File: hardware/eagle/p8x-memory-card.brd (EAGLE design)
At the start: 160 x 100 mm, 10 parts, among them J1 DIN41612-96M, U1 28C256-15, U2 62256-70, U3 74HCT245, U4 74HCT30, U5 74HCT138-DOE, U6 74HCT138-DLD, U7 74HCT00, U8 74HCT32, U9 74HCT08

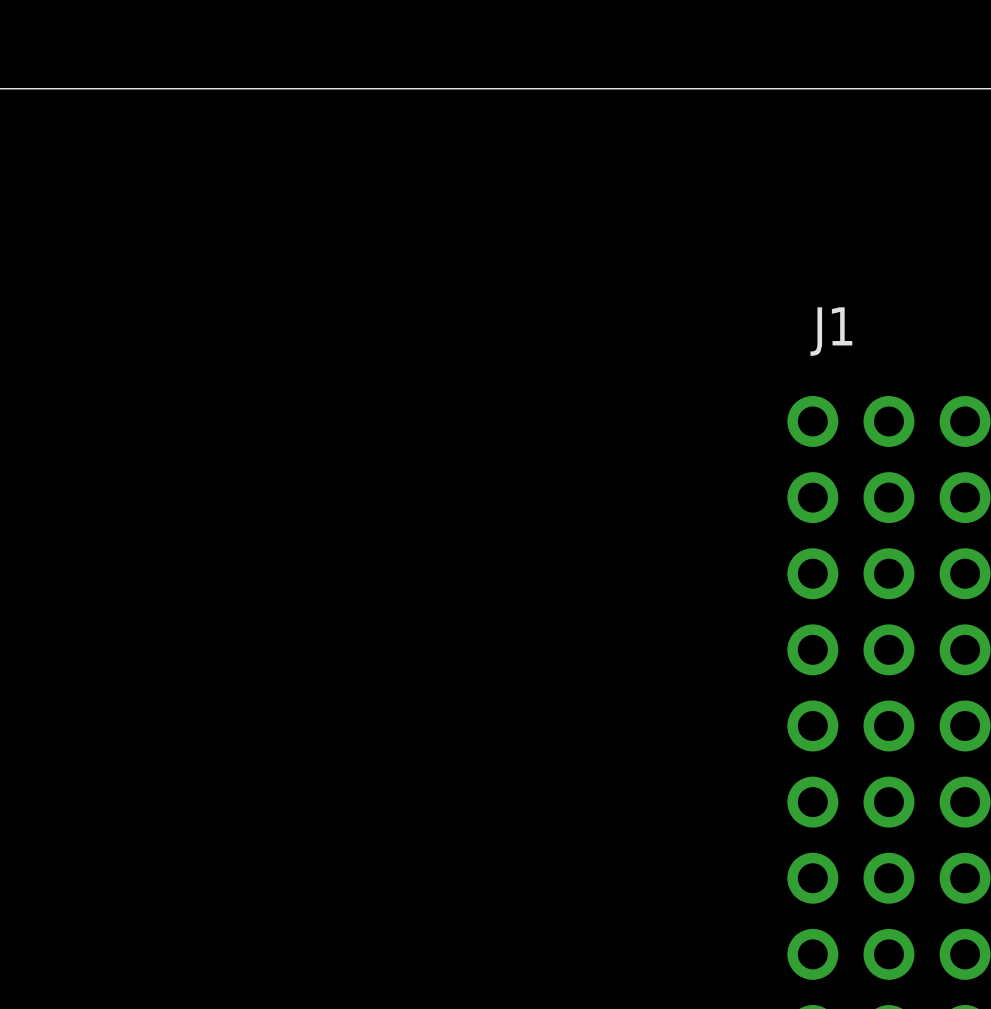
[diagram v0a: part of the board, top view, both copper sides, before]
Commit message: Memory card: ROM/RAM/RD/WR access LEDs replace SEL; traditional schematic PDFs; backlog + standards updates
- Select LEDs gated with -BOE (real accesses, not idle decode); spare U8/U9 gates as drivers
- Standards sec.9 allows finer-grained LED sets; fab checklist updated
- New traditional-style schematic PDFs + their render scripts (generators/)
- Backlog: DIN flange holes, board mounting holes, backplane PWR LED placement review
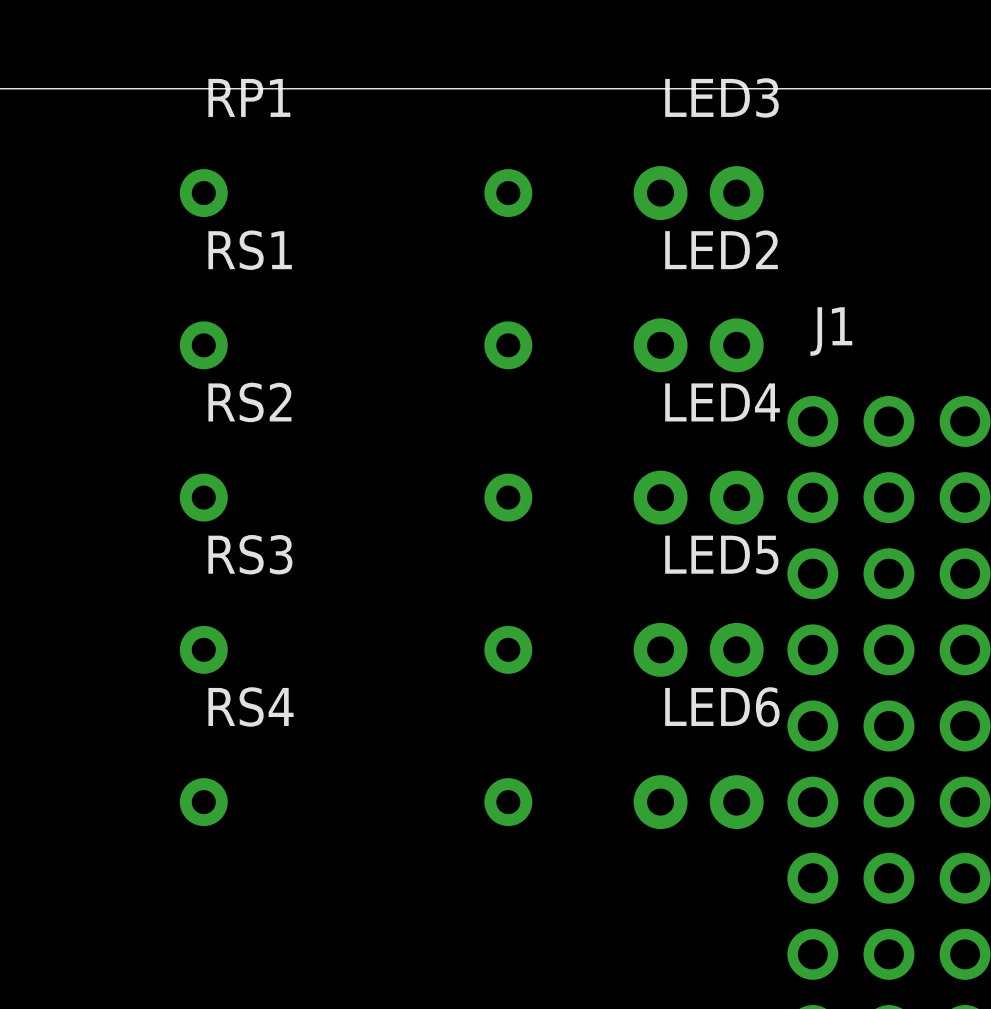
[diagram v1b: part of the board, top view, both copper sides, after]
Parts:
- added LED2: ROM-YEL, p8x:LED5
- added LED3: PWR-GRN, p8x:LED5
- added LED4: RAM-YEL, p8x:LED5
- added LED5: RD-GRN, p8x:LED5
- added LED6: WR-RED, p8x:LED5
- added RP1, RS1, RS2, RS3, RS4: 1K, p8x:R_AXIAL
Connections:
- new net LEDP: LED3.2, RP1.2
- new net LEDRA: LED4.2, RS2.2
- new net LEDRD: LED5.2, RS3.2
- new net LEDRO: LED2.2, RS1.2
- new net LEDWR: LED6.2, RS4.2
- new net RAMK: LED4.1, U8.6
- new net RDK: LED5.1, U9.6
- new net ROMK: LED2.1, U8.8
- new net WRK: LED6.1, U9.8
- net -BOE: now also U8.10, U8.5
- net -MEMW: now also U9.10, U9.9
- net -RAMCE: now also U8.4
- net -RD: now also U9.4, U9.5
- net A15: now also U8.9
- net GND: now also LED3.1; no longer U8.10, U8.4, U8.5, U8.9, U9.10, U9.4, U9.5, U9.9
- net VCC: now also RP1.1, RS1.1, RS2.1, RS3.1, RS4.1
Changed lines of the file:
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@@
 <element name="U8" library="p8x" package="DIP14" value="74HCT32" x="68.58" y="35.56"/>
 <element name="U9" library="p8x" package="DIP14" value="74HCT08" x="88.90" y="35.56"/>
+<element name="RP1" library="p8x" package="R_AXIAL" value="1K" x="127.00" y="96.52"/>
+<element name="LED3" library="p8x" package="LED5" value="PWR-GRN" x="142.24" y="96.52"/>
+<element name="RS1" library="p8x" package="R_AXIAL" value="1K" x="127.00" y="91.44"/>
+<element name="LED2" library="p8x" package="LED5" value="ROM-YEL" x="142.24" y="91.44"/>
+<element name="RS2" library="p8x" package="R_AXIAL" value="1K" x="127.00" y="86.36"/>
+<element name="LED4" library="p8x" package="LED5" value="RAM-YEL" x="142.24" y="86.36"/>
+<element name="RS3" library="p8x" package="R_AXIAL" value="1K" x="127.00" y="81.28"/>
+<element name="LED5" library="p8x" package="LED5" value="RD-GRN" x="142.24" y="81.28"/>
+<element name="RS4" library="p8x" package="R_AXIAL" value="1K" x="127.00" y="76.20"/>
+<element name="LED6" library="p8x" package="LED5" value="WR-RED" x="142.24" y="76.20"/>
 </elements><signals>
 <signal name="-BOE">
 <contactref element="U9" pad="3"/>
 <contactref element="U3" pad="19"/>
+<contactref element="U8" pad="5"/>
+<contactref element="U8" pad="10"/>
 </signal>
 <signal name="-IOPG">
@@
 <contactref element="U8" pad="1"/>
 <contactref element="U9" pad="2"/>
+<contactref element="U9" pad="9"/>
+<contactref element="U9" pad="10"/>
 </signal>
 <signal name="-RAMCE">
 <contactref element="U7" pad="3"/>
 <contactref element="U2" pad="20"/>
+<contactref element="U8" pad="4"/>
 </signal>
 <signal name="-RD">
@@
 <contactref element="U3" pad="1"/>
 <contactref element="U9" pad="1"/>
+<contactref element="U9" pad="4"/>
+<contactref element="U9" pad="5"/>
 </signal>
 <signal name="-WE">
@@
 <contactref element="U1" pad="20"/>
 <contactref element="U7" pad="1"/>
+<contactref element="U8" pad="9"/>
 </signal>
 <signal name="A2">
@@
 <contactref element="U7" pad="12"/>
 <contactref element="U7" pad="13"/>
-<contactref element="U8" pad="4"/>
-<contactref element="U8" pad="5"/>
-<contactref element="U8" pad="9"/>
-<contactref element="U8" pad="10"/>
 <contactref element="U8" pad="12"/>
 <contactref element="U8" pad="13"/>
-<contactref element="U9" pad="4"/>
-<contactref element="U9" pad="5"/>
-<contactref element="U9" pad="9"/>
-<contactref element="U9" pad="10"/>
 <contactref element="U9" pad="12"/>
 <contactref element="U9" pad="13"/>
+<contactref element="LED3" pad="1"/>
 <polygon width="0.254" layer="2" isolate="0.3" rank="1">
 <vertex x="0" y="0"/>
@@
 </polygon>
 </signal>
+<signal name="LEDP">
+<contactref element="RP1" pad="2"/>
+<contactref element="LED3" pad="2"/>
+</signal>
+<signal name="LEDRA">
+<contactref element="RS2" pad="2"/>
+<contactref element="LED4" pad="2"/>
+</signal>
+<signal name="LEDRD">
+<contactref element="RS3" pad="2"/>
+<contactref element="LED5" pad="2"/>
+</signal>
+<signal name="LEDRO">
+<contactref element="RS1" pad="2"/>
+<contactref element="LED2" pad="2"/>
+</signal>
+<signal name="LEDWR">
+<contactref element="RS4" pad="2"/>
+<contactref element="LED6" pad="2"/>
+</signal>
 <signal name="MD0">
 <contactref element="U3" pad="18"/>
@@
 <contactref element="U1" pad="19"/>
 <contactref element="U2" pad="19"/>
+</signal>
+<signal name="RAMK">
+<contactref element="U8" pad="6"/>
+<contactref element="LED4" pad="1"/>
+</signal>
+<signal name="RDK">
+<contactref element="U9" pad="6"/>
+<contactref element="LED5" pad="1"/>
+</signal>
+<signal name="ROMK">
+<contactref element="U8" pad="8"/>
+<contactref element="LED2" pad="1"/>
 </signal>
 <signal name="VCC">
@@
 <contactref element="U8" pad="14"/>
 <contactref element="U9" pad="14"/>
+<contactref element="RP1" pad="1"/>
+<contactref element="RS1" pad="1"/>
+<contactref element="RS2" pad="1"/>
+<contactref element="RS3" pad="1"/>
+<contactref element="RS4" pad="1"/>
 <polygon width="0.254" layer="15" isolate="0.3" rank="1">
 <vertex x="0" y="0"/>
@@
 </polygon>
 </signal>
+<signal name="WRK">
+<contactref element="U9" pad="8"/>
+<contactref element="LED6" pad="1"/>
+</signal>
 </signals></board></drawing></eagle>
